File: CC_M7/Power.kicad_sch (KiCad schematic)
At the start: 0 parts

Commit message: update
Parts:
- added C28: 10uF, symbol Device:C
- added C29: 430pF, symbol Device:C
- added C30: 47uF, symbol Device:C
- added PS1: TPS82140SILR, TPS82140SILR:CONV_TPS82140SILR, symbol TPS82140SILR:TPS82140SILR
- added R10: 10k, symbol Device:R
- added R11: 523k, symbol Device:R
- added R15: 100k, symbol Device:R
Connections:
- new net: PS1.6 (FB), R11.1, R15.2
- new net: C29.1, PS1.8 (SS/TR)
- new net: PS1.7 (PG), R10.1
- new net GND: C28.1, C28.2, C29.2, C30.1, C30.2, PS1.1 (EN), PS1.10 (GND), PS1.11 (GND), PS1.12 (GND), PS1.2 (VIN), PS1.3 (GND), PS1.4 (VOUT), PS1.5 (VOUT), PS1.9 (GND), R10.2, R11.2, R15.1
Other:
- company: (none) -> YENIAY
- title: (none) -> POWER SECTION

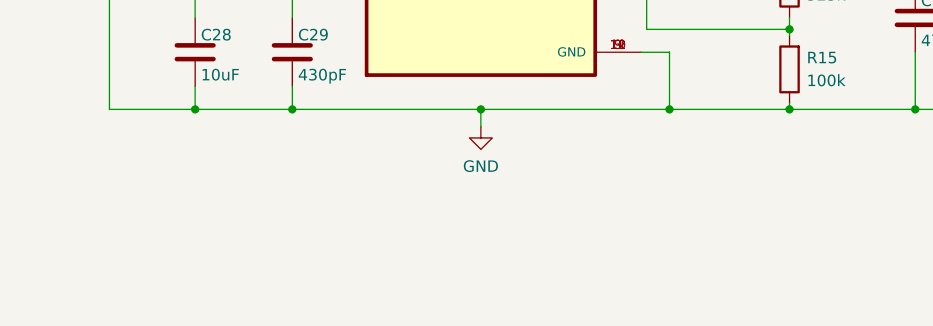
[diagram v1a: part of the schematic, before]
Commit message: update schematic
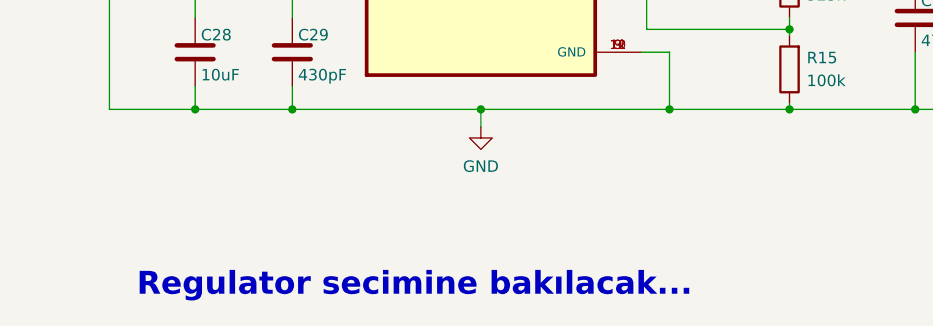
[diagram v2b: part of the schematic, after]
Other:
- note added: "Regulator secimine bakılacak..."
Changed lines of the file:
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@@
+		)
+	)
+	(text "Regulator secimine bakılacak..."
+		(exclude_from_sim no)
+		(at 75.184 83.058 0)
+		(effects
+			(font
+				(size 2.54 2.54)
+				(thickness 0.508)
+				(bold yes)
+			)
 		)
 	)

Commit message: Connectors updated
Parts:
- removed C28: 10uF, symbol Device:C
- removed C29: 430pF, symbol Device:C
- removed C30: 47uF, symbol Device:C
- removed PS1: TPS82140SILR, TPS82140SILR:CONV_TPS82140SILR, symbol TPS82140SILR:TPS82140SILR
- removed R11: 523k, symbol Device:R
- removed R15: 100k, symbol Device:R
- added C43: 22uF, symbol Device:C
- added C47: 100uF, symbol Device:C
- added C48: 68pF, symbol Device:C
- added C49: 47uF, symbol Device:C
- added L5: 10uH, symbol Device:L
- added R12: 100k, symbol Device:R
- added R13: 13.7k, symbol Device:R
- added U8: TPS54202DDCR, TPS54202DDCR:SOT95P280X110-6N, symbol TPS54202DDCR:TPS54202DDCR
- R10: value 10k -> 0R
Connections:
- net GND: now also R10.1, C43.1, C43.2, C48.1, C49.1, C49.2, L5.2, R12.2, R13.1, U8.1 (GND), U8.3 (VIN); no longer R10.2
- new net: C47.2, L5.1, U8.2 (SW)
- new net: C47.1, U8.6 (BOOT)
- new net +5V: R10.2
- new net FB: C48.2, R12.1, R13.2, U8.4 (FB)
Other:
- note added: "TPS54202DDCR"
- note added: "VINMIN 6V VINMAX 15V VOUT 5V IOUT 2A"
- note removed: "Regulator secimine bakılacak..."

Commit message: nrf
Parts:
- added C30, C45, C46, C50: 1uF, symbol Device:C_Small
- added U10, U9: ME6211C33M5, Package_TO_SOT_SMD:SOT-23-5, symbol Regulator_Linear:ME6211C33M5
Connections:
- net +5V: now also C30.1, C46.1, U10.1 (V_{IN}), U10.3 (CE), U9.1 (V_{IN}), U9.3 (CE)
- net GND: now also C30.2, C45.2, C46.2, C50.2, U10.2 (V_{SS}), U9.2 (V_{SS})
- new net +3.3V: C45.1, U9.5 (V_{OUT})
- new net 3V3_RF: C50.1, U10.5 (V_{OUT})
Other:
- moved on the sheet: C43, C47, C48, C49, L5, R10, R12, R13, U8

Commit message: final schematic 6 warning
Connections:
- no-connect marks 0 -> 1
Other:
- moved on the sheet: C43, C48, L5, R10, R12

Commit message: schematic control comment
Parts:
- added J1: Conn_01x02_Pin, symbol Connector:Conn_01x02_Pin
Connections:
- net GND: now also J1.2 (Pin_2); no longer C43.1, U8.3 (VIN)
- new net VIN: C43.1, J1.1 (Pin_1), U8.3 (VIN)
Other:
- note added: "*2A dayanıklı connector secilecek."
- note added: "DEVRE KONTROL EDILECEK!!!!!"
- note added: "YENIAY"
- company: YENIAY -> (none)
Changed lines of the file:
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@@
 	(title_block
 		(title "POWER SECTION")
-		(company "YENIAY")
 	)
 	(junction
@@
 	)
 	(junction
-		(at 38.1 40.64)
-		(diameter 0)
-		(color 0 0 0 0)
-	)
-	(junction
 		(at 44.45 40.64)
 		(diameter 0)
@@
 	)
 	(junction
-		(at 44.45 60.96)
-		(diameter 0)
-		(color 0 0 0 0)
-	)
-	(junction
 		(at 138.43 38.1)
 		(diameter 0)
@@
 	(wire
 		(pts
+			(xy 109.22 185.42) (xy 109.22 182.88)
+		)
+		(stroke
+			(width 0)
+			(type default)
+		)
+	)
+	(wire
+		(pts
 			(xy 99.06 48.26) (xy 99.06 60.96)
 		)
@@
 	(wire
 		(pts
+			(xy 109.22 187.96) (xy 109.22 190.5)
+		)
+		(stroke
+			(width 0)
+			(type default)
+		)
+	)
+	(wire
+		(pts
 			(xy 74.93 135.89) (xy 74.93 139.7)
 		)
@@
 	(wire
 		(pts
-			(xy 33.02 40.64) (xy 38.1 40.64)
-		)
-		(stroke
-			(width 0)
-			(type default)
-		)
-	)
-	(wire
-		(pts
 			(xy 138.43 60.96) (xy 99.06 60.96)
 		)
@@
 		)
 	)
+	(bus
+		(pts
+			(xy 12.7 210.82) (xy 198.12 210.82)
+		)
+		(stroke
+			(width 0)
+			(type dash)
+		)
+	)
 	(wire
 		(pts
@@
 	(wire
 		(pts
-			(xy 38.1 60.96) (xy 44.45 60.96)
-		)
-		(stroke
-			(width 0)
-			(type default)
-		)
-	)
-	(wire
-		(pts
-			(xy 38.1 40.64) (xy 38.1 60.96)
-		)
-		(stroke
-			(width 0)
-			(type default)
-		)
-	)
-	(wire
-		(pts
 			(xy 128.27 38.1) (xy 138.43 38.1)
 		)
@@
 	(wire
 		(pts
-			(xy 38.1 40.64) (xy 44.45 40.64)
+			(xy 33.02 40.64) (xy 44.45 40.64)
 		)
 		(stroke
@@
 		)
 	)
+	(bus
+		(pts
+			(xy 11.43 160.02) (xy 199.39 160.02)
+		)
+		(stroke
+			(width 0)
+			(type dash)
+		)
+	)
 	(wire
 		(pts
@@
 	(wire
 		(pts
+			(xy 101.6 185.42) (xy 109.22 185.42)
+		)
+		(stroke
+			(width 0)
+			(type default)
+		)
+	)
+	(wire
+		(pts
 			(xy 148.59 60.96) (xy 138.43 60.96)
 		)
@@
 	(wire
 		(pts
+			(xy 101.6 187.96) (xy 109.22 187.96)
+		)
+		(stroke
+			(width 0)
+			(type default)
+		)
+	)
+	(wire
+		(pts
 			(xy 43.18 127) (xy 43.18 129.54)
 		)
@@
 			(width 0)
 			(type default)
+		)
+	)
+	(text "DEVRE KONTROL EDILECEK!!!!!"
+		(exclude_from_sim no)
+		(at 90.17 80.01 0)
+		(effects
+			(font
+				(size 2.54 2.54)
+				(thickness 0.508)
+				(bold yes)
+			)
+		)
+	)
+	(text "YENIAY"
+		(exclude_from_sim no)
+		(at 109.22 262.89 0)
+		(effects
+			(font
+				(size 7.62 7.62)
+				(bold yes)
+				(italic yes)
+			)
 		)
 	)
@@
 			)
 			(justify left)
+		)
+	)
+	(text "*2A dayanıklı connector secilecek."
+		(exclude_from_sim no)
+		(at 101.6 201.93 0)
+		(effects
+			(font
+				(size 1.27 1.27)
+			)
 		)
 	)
@@
 		)
 	)
+	(global_label "VIN"
+		(shape input)
+		(at 109.22 182.88 90)
+		(fields_autoplaced yes)
+		(effects
+			(font
+				(size 1.27 1.27)
+			)
+			(justify left)
+		)
+		(property "Intersheetrefs" "${INTERSHEET_REFS}"
+			(at 109.22 176.8709 90)
+			(effects
+				(font
+					(size 1.27 1.27)
+				)
+				(justify left)
+				(hide yes)
+			)
+		)
+	)
 	(global_label "3V3_RF"
 		(shape input)
@@
 	)
 	(symbol
+		(lib_id "Connector:Conn_01x02_Pin")
+		(at 96.52 185.42 0)
+		(unit 1)
+		(exclude_from_sim no)
+		(in_bom yes)
+		(on_board yes)
+		(dnp no)
+		(fields_autoplaced yes)
+		(property "Reference" "J1"
+			(at 97.155 180.34 0)
+			(effects
+				(font
+					(size 1.27 1.27)
+				)
+			)
+		)
+		(property "Value" "Conn_01x02_Pin"
+			(at 97.155 182.88 0)
+			(effects
+				(font
+					(size 1.27 1.27)
+				)
+			)
+		)
+		(property "Footprint" ""
+			(at 96.52 185.42 0)
+			(effects
+				(font
+					(size 1.27 1.27)
+				)
+				(hide yes)
+			)
+		)
+		(property "Datasheet" "~"
+			(at 96.52 185.42 0)
+			(effects
+				(font
+					(size 1.27 1.27)
+				)
+				(hide yes)
+			)
+		)
+		(property "Description" "Generic connector, single row, 01x02, script generated"
+			(at 96.52 185.42 0)
+			(effects
+				(font
+					(size 1.27 1.27)
+				)
+				(hide yes)
+			)
+		)
+		(pin "1"
+		)
+		(pin "2"
+		)
+		(instances
+			(project ""
+				(path "/20c3bbae-00c6-470e-8b69-dc0f665257a3/d5e2a406-9a7f-4b4d-9070-1dc6f1aabbf7"
+					(reference "J1")
+					(unit 1)
+				)
+			)
+		)
+	)
+	(symbol
 		(lib_id "power:GND")
 		(at 140.97 140.97 0)
@@
 					(unit 1)
 				)
+			)
+		)
+	)
+	(symbol
+		(lib_id "power:GND")
+		(at 109.22 190.5 0)
+		(unit 1)
+		(exclude_from_sim no)
+		(in_bom yes)
+		(on_board yes)
+		(dnp no)
+		(fields_autoplaced yes)
+		(property "Reference" "#PWR026"
+			(at 109.22 196.85 0)
+			(effects
+				(font
+					(size 1.27 1.27)
+				)
+				(hide yes)
+			)
+		)
+		(property "Value" "GND"
+			(at 109.22 195.58 0)
+			(effects
+				(font
+					(size 1.27 1.27)
+				)
+			)
+		)
+		(property "Footprint" ""
+			(at 109.22 190.5 0)
+			(effects
+				(font
+					(size 1.27 1.27)
+				)
+				(hide yes)
+			)
+		)
+		(property "Datasheet" ""
+			(at 109.22 190.5 0)
+			(effects
+				(font
+					(size 1.27 1.27)
+				)
+				(hide yes)
+			)
+		)
+		(property "Description" "Power symbol creates a global label with name \"GND\" , ground"
+			(at 109.22 190.5 0)
+			(effects
+				(font
+					(size 1.27 1.27)
+				)
+				(hide yes)
+			)
+		)
+		(pin "1"
+		)
+		(instances
+			(project "CC_M7"
+				(path "/20c3bbae-00c6-470e-8b69-dc0f665257a3/d5e2a406-9a7f-4b4d-9070-1dc6f1aabbf7"
+					(reference "#PWR026")
+					(unit 1)
+				)

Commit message: Changes updated @ CCM7.docx
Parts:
- removed J1: Conn_01x02_Pin, symbol Connector:Conn_01x02_Pin
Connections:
- net FB renamed TPS5420_FB
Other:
- note removed: "*2A dayanıklı connector secilecek."

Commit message: Footprint assignment 1/2
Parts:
- C30, C45, C46, C50: footprint (none) -> Capacitor_SMD:C_0805_2012Metric
- C43, C49: footprint (none) -> Capacitor_SMD:C_1210_3225Metric
- C47: value 100uF -> 100nF; footprint (none) -> Capacitor_SMD:C_1210_3225Metric
- C48: footprint (none) -> Capacitor_SMD:C_0402_1005Metric
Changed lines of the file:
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@@
 			)
 		)
-		(property "Footprint" ""
+		(property "Footprint" "Capacitor_SMD:C_0805_2012Metric"
 			(at 157.48 134.62 0)
 			(effects
@@
 			)
 		)
-		(property "Value" "100uF"
+		(property "Value" "100nF"
 			(at 108.585 32.385 90)
 			(effects
@@
 			)
 		)
-		(property "Footprint" ""
+		(property "Footprint" "Capacitor_SMD:C_1210_3225Metric"
 			(at 106.68 34.5948 0)
 			(effects
@@
 			)
 		)
-		(property "Footprint" ""
+		(property "Footprint" "Capacitor_SMD:C_0402_1005Metric"
 			(at 129.2352 46.99 0)
 			(effects
@@
 			)
 		)
-		(property "Footprint" ""
+		(property "Footprint" "Capacitor_SMD:C_0805_2012Metric"
 			(at 43.18 134.62 0)
 			(effects
@@
 			)
 		)
-		(property "Footprint" ""
+		(property "Footprint" "Capacitor_SMD:C_0805_2012Metric"
 			(at 74.93 133.35 0)
 			(effects
@@
 			)
 		)
-		(property "Footprint" ""
+		(property "Footprint" "Capacitor_SMD:C_1210_3225Metric"
 			(at 45.4152 54.61 0)
 			(effects
@@
 			)
 		)
-		(property "Footprint" ""
+		(property "Footprint" "Capacitor_SMD:C_1210_3225Metric"
 			(at 149.5552 53.34 0)
 			(effects
@@
 			)
 		)
-		(property "Footprint" ""
+		(property "Footprint" "Capacitor_SMD:C_0805_2012Metric"
 			(at 125.73 135.89 0)
 			(effects
